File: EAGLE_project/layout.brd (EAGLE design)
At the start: 100 x 80 mm, 15 parts

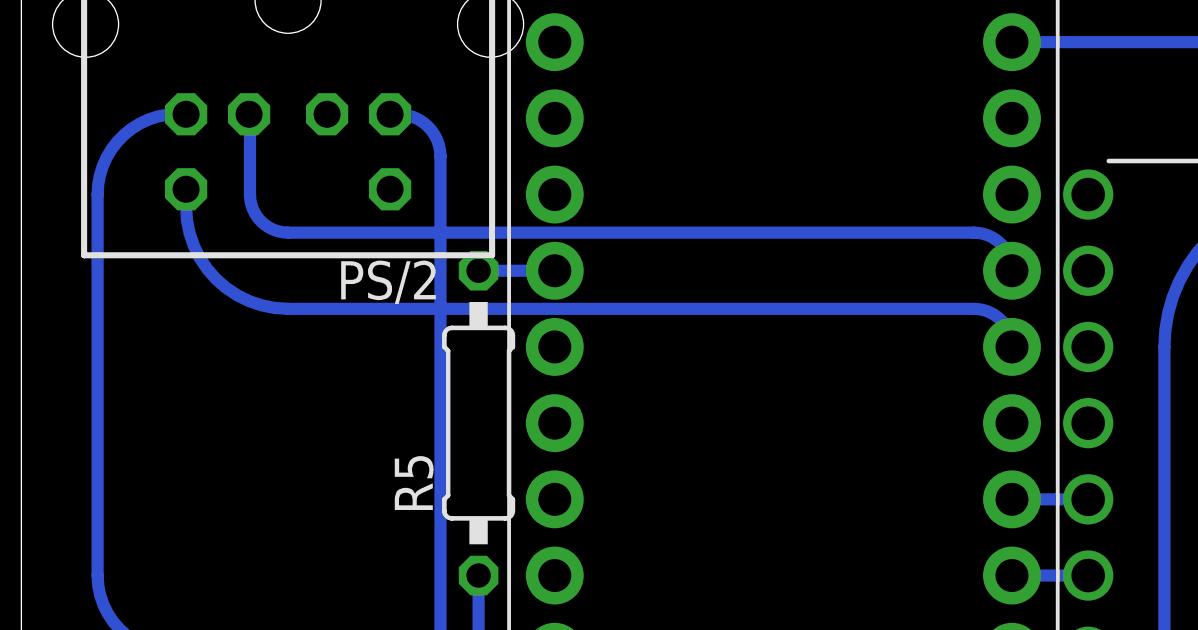
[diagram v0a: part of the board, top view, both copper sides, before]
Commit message: Change TrackPoint CLK from Arduino pin 8 to 7
This is to have it on an interrupt, necessary for stream mode.
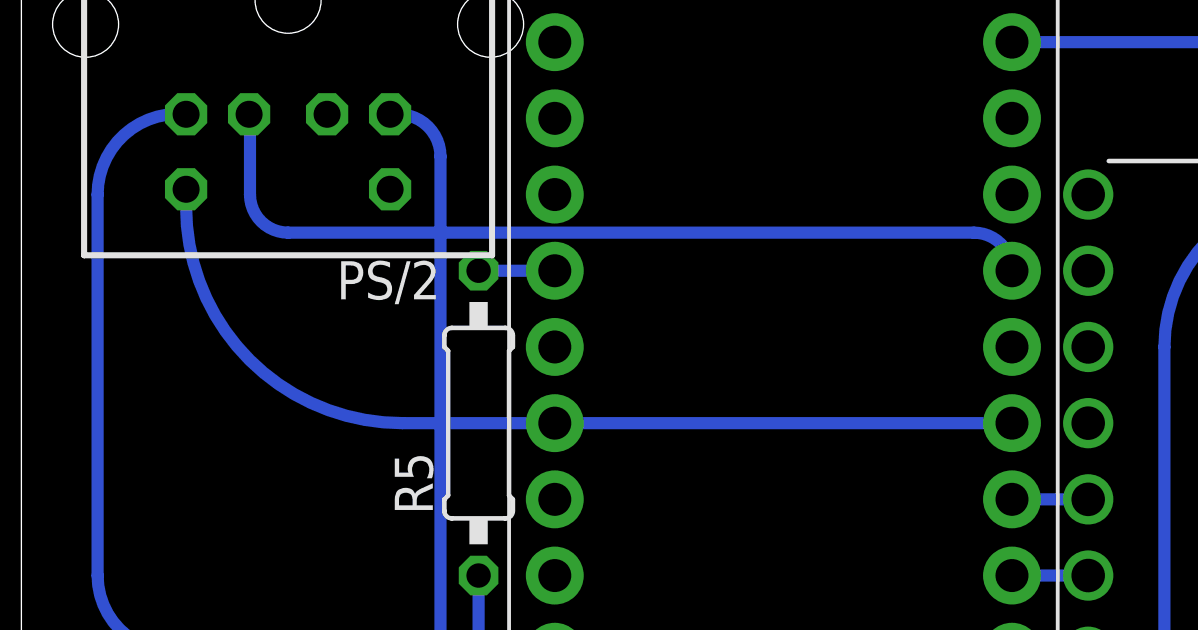
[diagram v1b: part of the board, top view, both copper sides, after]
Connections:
- net +CLK: now also U$2.P$6; no longer U$2.P$5
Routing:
- net +CLK: track 30.1 -> 31.1 mm
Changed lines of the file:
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@@
 </signal>
 <signal name="+CLK">
-<contactref element="U$2" pad="P$5"/>
 <contactref element="PS/2" pad="5"/>
-<wire x1="31.75" y1="64.77" x2="8.89" y2="64.77" width="0.4064" layer="16"/>
-<wire x1="8.89" y1="64.77" x2="5.49" y2="68.17" width="0.4064" layer="16" curve="-90"/>
+<contactref element="U$2" pad="P$6"/>
+<wire x1="33.02" y1="60.96" x2="12.7" y2="60.96" width="0.4064" layer="16"/>
+<wire x1="12.7" y1="60.96" x2="5.49" y2="68.17" width="0.4064" layer="16" curve="-90"/>
 <wire x1="5.49" y1="68.17" x2="5.49" y2="68.756" width="0.4064" layer="16"/>
-<wire x1="31.75" y1="64.77" x2="33.02" y2="63.5" width="0.4064" layer="16" curve="-90"/>
 </signal>
 <signal name="+DATA">

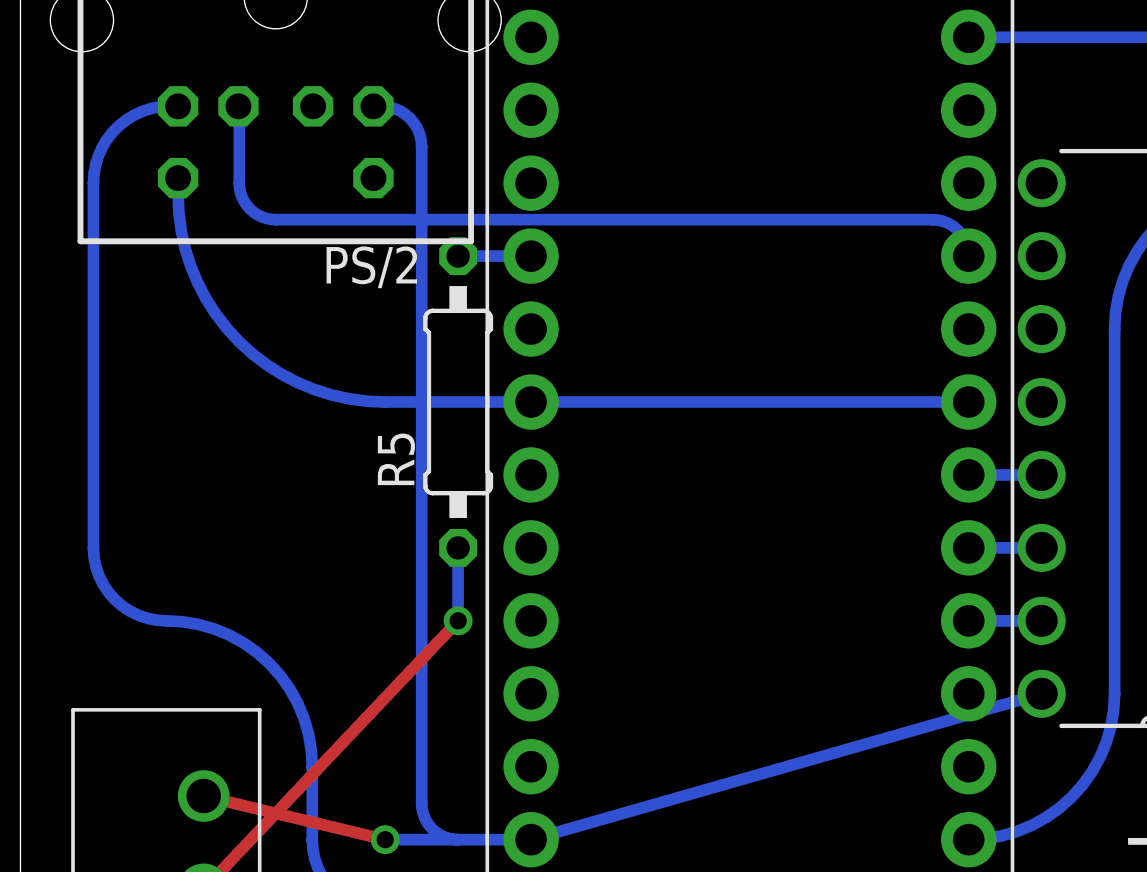
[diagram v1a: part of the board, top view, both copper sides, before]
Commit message: Change TrackPoint CLK from Arduino pin 7 to 3
With pin 7, when lifting the finger from the TrackPoint, then cursor movement
doesn't stop. This happens with the following library and the issue is
confirmed by its author.

https://github.com/rampadc/arduino-trackpoint-extended
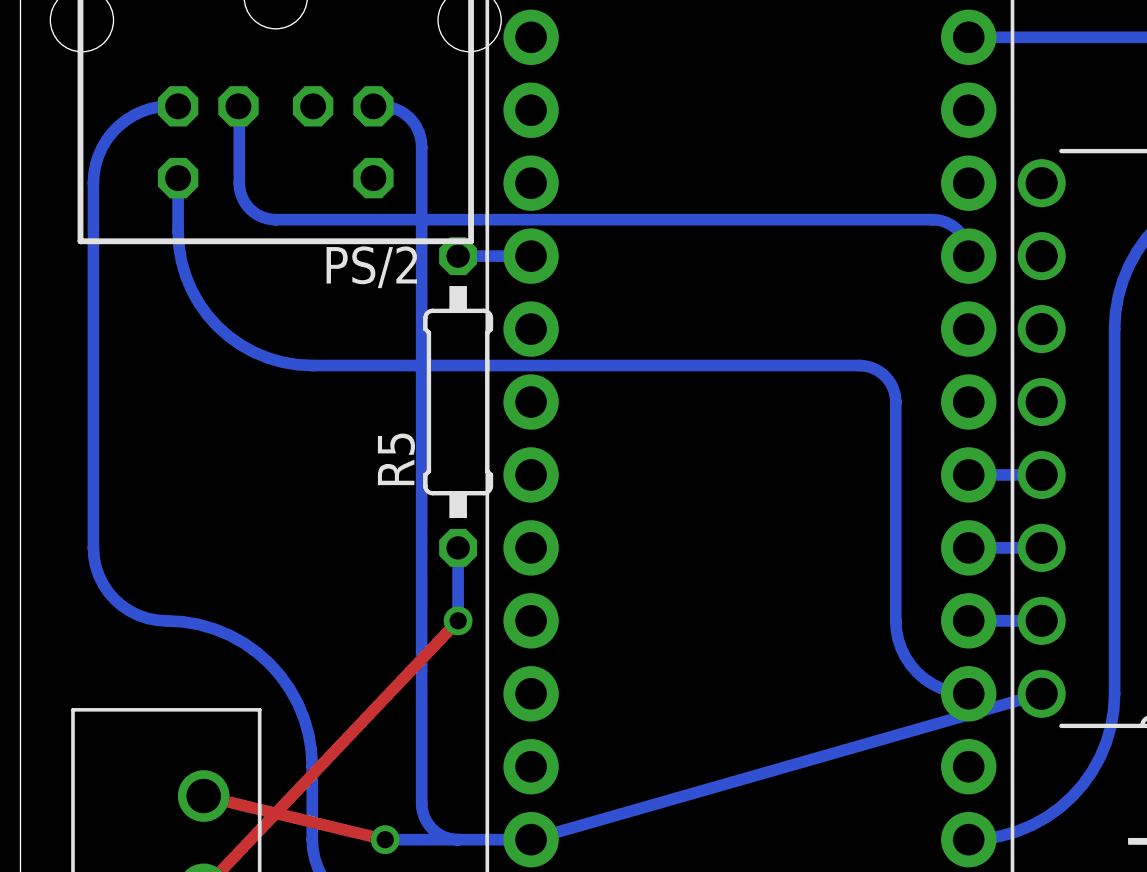
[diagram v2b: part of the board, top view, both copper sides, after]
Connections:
- net +CLK: now also U$2.P$10; no longer U$2.P$6
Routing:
- net +CLK: track 31.1 -> 40.5 mm
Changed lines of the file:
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@@
 <signal name="+CLK">
 <contactref element="PS/2" pad="5"/>
-<contactref element="U$2" pad="P$6"/>
-<wire x1="33.02" y1="60.96" x2="12.7" y2="60.96" width="0.4064" layer="16"/>
-<wire x1="12.7" y1="60.96" x2="5.49" y2="68.17" width="0.4064" layer="16" curve="-90"/>
-<wire x1="5.49" y1="68.17" x2="5.49" y2="68.756" width="0.4064" layer="16"/>
+<contactref element="U$2" pad="P$10"/>
+<wire x1="5.49" y1="68.756" x2="5.49" y2="66.9" width="0.4064" layer="16"/>
+<wire x1="5.49" y1="66.9" x2="10.16" y2="62.23" width="0.4064" layer="16" curve="90"/>
+<wire x1="10.16" y1="62.23" x2="29.21" y2="62.23" width="0.4064" layer="16"/>
+<wire x1="29.21" y1="62.23" x2="30.48" y2="60.96" width="0.4064" layer="16" curve="-90"/>
+<wire x1="30.48" y1="60.96" x2="30.48" y2="53.34" width="0.4064" layer="16"/>
+<wire x1="30.48" y1="53.34" x2="33.02" y2="50.8" width="0.4064" layer="16" curve="90"/>
 </signal>
 <signal name="+DATA">
